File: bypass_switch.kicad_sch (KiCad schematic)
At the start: 13 parts, among them J1 Footswitch_conn_01x02, J4 LED_conn_01x02, K2 HFD4/9-S1, Q1 2N3904, U1 NE555DR

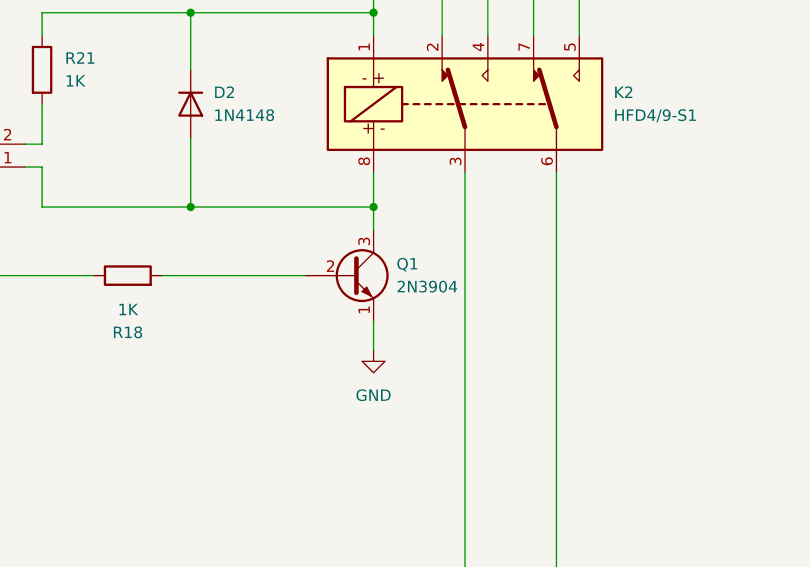
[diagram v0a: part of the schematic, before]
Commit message: added LCSC part numbers
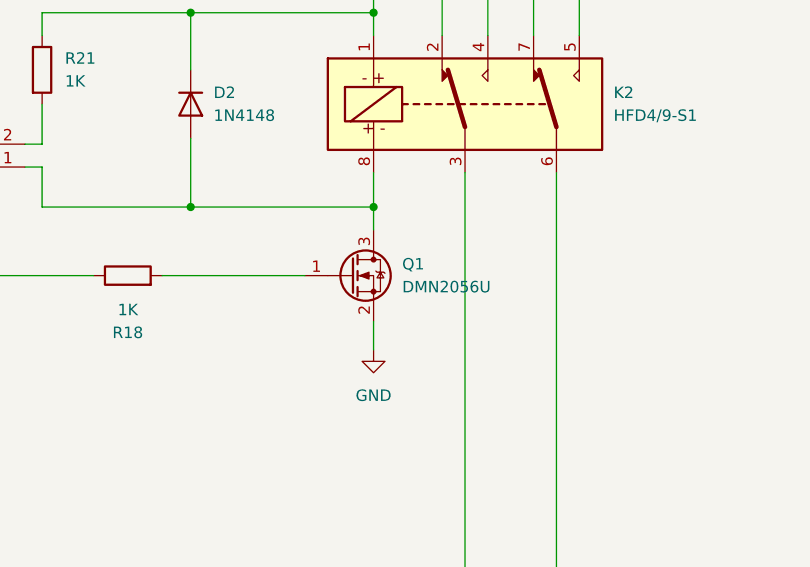
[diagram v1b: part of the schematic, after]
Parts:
- removed Q1: 2N3904, Package_TO_SOT_THT:TO-92_Inline, symbol Transistor_BJT:2N3904
- added Q1: DMN2056U, Package_TO_SOT_SMD:SOT-23, symbol Transistor_FET:DMN2056U
- C14: LCSC (none) -> C476766
- R1, R2: LCSC (none) -> C2930231
- R18, R21: LCSC (none) -> C2907295
- R3: LCSC (none) -> C2907293
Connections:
- net GND: now also Q1.2 (S)
- net at D2.2 (A), J4.1 (Pin_1), K2.8: now also Q1.3 (D)
- net at R18.2: now also Q1.1 (G)
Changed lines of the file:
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@@
+      (effects (font (size 1.27 1.27)) hide)
+    )
+    (property "LCSC" "~" (at 151.13 66.675 0)
       (effects (font (size 1.27 1.27)) hide)
     )
@@
     )
   )
+  (symbol (lib_id "Transistor_FET:DMN2056U") (at 192.405 78.74 0) (unit 1)
+    (in_bom yes) (on_board yes) (dnp no) (fields_autoplaced)
+    (property "Reference" "Q1" (at 198.12 77.47 0)
+      (effects (font (size 1.27 1.27)) (justify left))
+    )
+    (property "Value" "DMN2056U" (at 198.12 80.01 0)
+      (effects (font (size 1.27 1.27)) (justify left))
+    )
+    (property "Footprint" "Package_TO_SOT_SMD:SOT-23" (at 197.485 80.645 0)
+      (effects (font (size 1.27 1.27) italic) (justify left) hide)
+    )
+    (property "Datasheet" "http://www.diodes.com/assets/Datasheets/DMN2056U.pdf" (at 192.405 78.74 0)
+      (effects (font (size 1.27 1.27)) (justify left) hide)
+    )
+    (property "LCSC" "C332302" (at 192.405 78.74 0)
+      (effects (font (size 1.27 1.27)) hide)
+    )
+    (pin "1")
+    (pin "2")
+    (pin "3")
+    (instances
+      (project "plumeclone"
+        (path "/2b147e3f-6b4e-4bfa-a787-bdf6c0ff1658/bc03c5d7-4e4e-4635-a51f-453e9137cc72"
+          (reference "Q1") (unit 1)
+        )
+      )
+    )
+  )
   (symbol (lib_id "Device:R") (at 158.115 55.88 0) (unit 1)
     (in_bom yes) (on_board yes) (dnp no) (fields_autoplaced)
@@
       (effects (font (size 1.27 1.27)) hide)
     )
+    (property "LCSC" "C2907295" (at 158.115 55.88 0)
+      (effects (font (size 1.27 1.27)) hide)
+    )
     (pin "1")
     (pin "2")
@@
     )
   )
-  (symbol (lib_id "Transistor_BJT:2N3904") (at 192.405 78.74 0) (unit 1)
-    (in_bom yes) (on_board yes) (dnp no) (fields_autoplaced)
-    (property "Reference" "Q1" (at 197.485 77.47 0)
-      (effects (font (size 1.27 1.27)) (justify left))
-    )
-    (property "Value" "2N3904" (at 197.485 80.01 0)
-      (effects (font (size 1.27 1.27)) (justify left))
-    )
-    (property "Footprint" "Package_TO_SOT_THT:TO-92_Inline" (at 197.485 80.645 0)
-      (effects (font (size 1.27 1.27) italic) (justify left) hide)
-    )
-    (property "Datasheet" "https://www.onsemi.com/pub/Collateral/2N3903-D.PDF" (at 192.405 78.74 0)
-      (effects (font (size 1.27 1.27)) (justify left) hide)
-    )
-    (pin "1")
-    (pin "2")
-    (pin "3")
-    (instances
-      (project "plumeclone"
-        (path "/2b147e3f-6b4e-4bfa-a787-bdf6c0ff1658/bc03c5d7-4e4e-4635-a51f-453e9137cc72"
-          (reference "Q1") (unit 1)
-        )
-      )
-    )
-  )
   (symbol (lib_id "power:GND") (at 92.71 55.88 0) (unit 1)
     (in_bom yes) (on_board yes) (dnp no) (fields_autoplaced)
@@
     )
     (property "Datasheet" "~" (at 64.77 92.71 0)
+      (effects (font (size 1.27 1.27)) hide)
+    )
+    (property "LCSC" "C2930231" (at 64.77 92.71 0)
       (effects (font (size 1.27 1.27)) hide)
     )
@@
       (effects (font (size 1.27 1.27)) hide)
     )
-    (property "LCSC" "" (at 92.71 49.53 0)
+    (property "LCSC" "C476766" (at 92.71 49.53 0)
       (effects (font (size 1.27 1.27)) hide)
     )
@@
     )
     (property "Datasheet" "~" (at 64.77 71.12 0)
+      (effects (font (size 1.27 1.27)) hide)
+    )
+    (property "LCSC" "C2930231" (at 64.77 71.12 0)
       (effects (font (size 1.27 1.27)) hide)
     )
@@
     )
     (property "Datasheet" "~" (at 73.66 120.65 0)
+      (effects (font (size 1.27 1.27)) hide)
+    )
+    (property "LCSC" "~" (at 73.66 120.65 0)
       (effects (font (size 1.27 1.27)) hide)
     )
@@
       (effects (font (size 1.27 1.27)) hide)
     )
+    (property "LCSC" "C2907295" (at 167.64 78.74 0)
+      (effects (font (size 1.27 1.27)) hide)
+    )
     (pin "1")
     (pin "2")
@@
       (effects (font (size 1.27 1.27)) hide)
     )
+    (property "LCSC" "C2907293" (at 107.95 95.25 0)
+      (effects (font (size 1.27 1.27)) hide)
+    )

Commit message: added schema pdf
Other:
- title: (none) -> EQD Plume Clone
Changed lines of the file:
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@@
 (kicad_sch (version 20230121) (generator eeschema)
   (paper "A4")
+  (title_block
+    (title "EQD Plume Clone")
+    (date "2023-08-31")
+    (rev "A")
+  )
   (junction (at 87.63 43.18) (diameter 0) (color 0 0 0 0)
   )
